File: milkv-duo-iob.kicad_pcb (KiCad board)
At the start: 2 copper layers, 71.6 x 57.7 mm, 15 parts, among them J1 8P8C_Shielded, J2 Conn_01x20, J3 Conn_01x20, J4 Conn_01x12, J5 Conn_01x12, J6 Conn_01x04, SW1 SW_Push, SW2 SW_Push, U1 Milk-V Duo

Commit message: Rev.B
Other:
- board text added: "Milk-V Duo IO Board Rev.B 2024-09-24 @myon___"
- board text removed: "Milk-V Duo IO Board Rev.A 2024-09-21 @myon___"
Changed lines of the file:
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@@
 		)
 	)
-	(gr_text "Milk-V Duo IO Board Rev.A\n2024-09-21 @myon___"
+	(gr_text "Milk-V Duo IO Board Rev.B\n2024-09-24 @myon___"
 		(at 129.54 102.87 0)
 		(layer "F.SilkS")

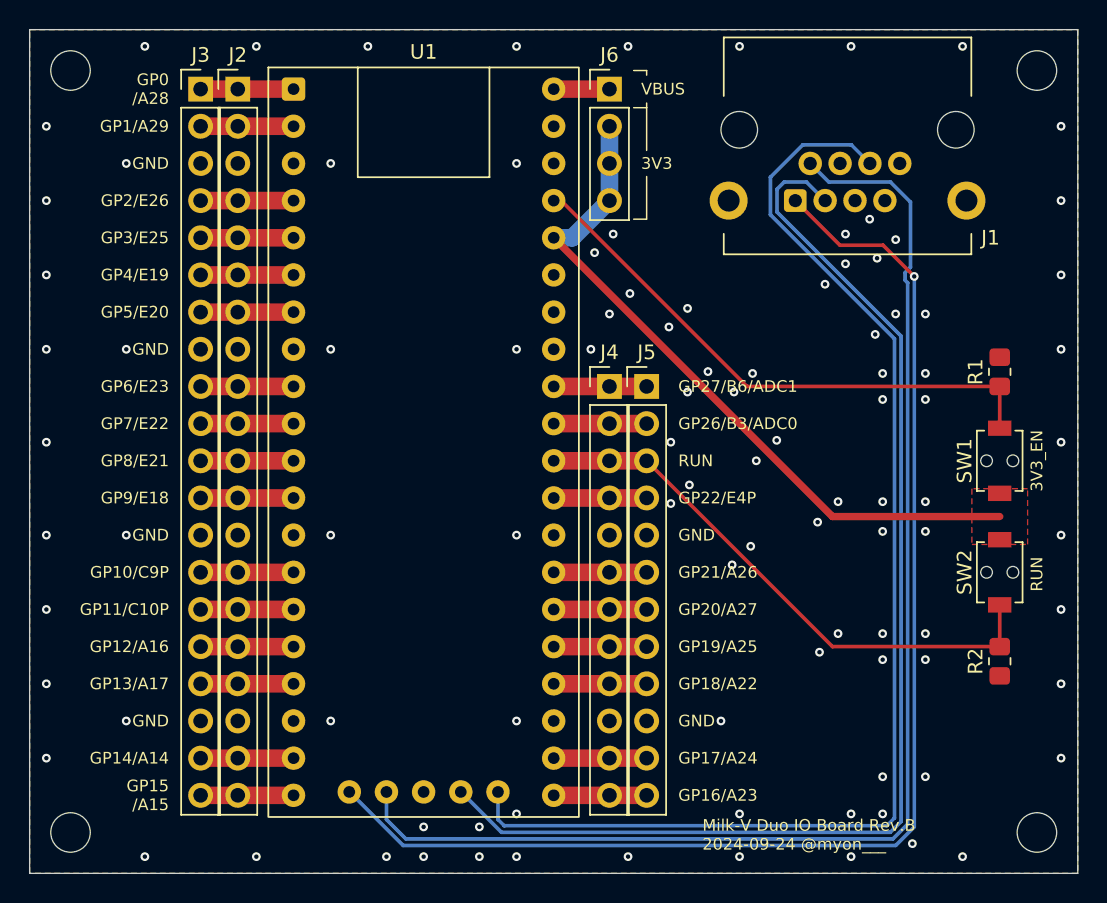
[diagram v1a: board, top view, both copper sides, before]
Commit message: Improve impedance of Etherer (hopefully)
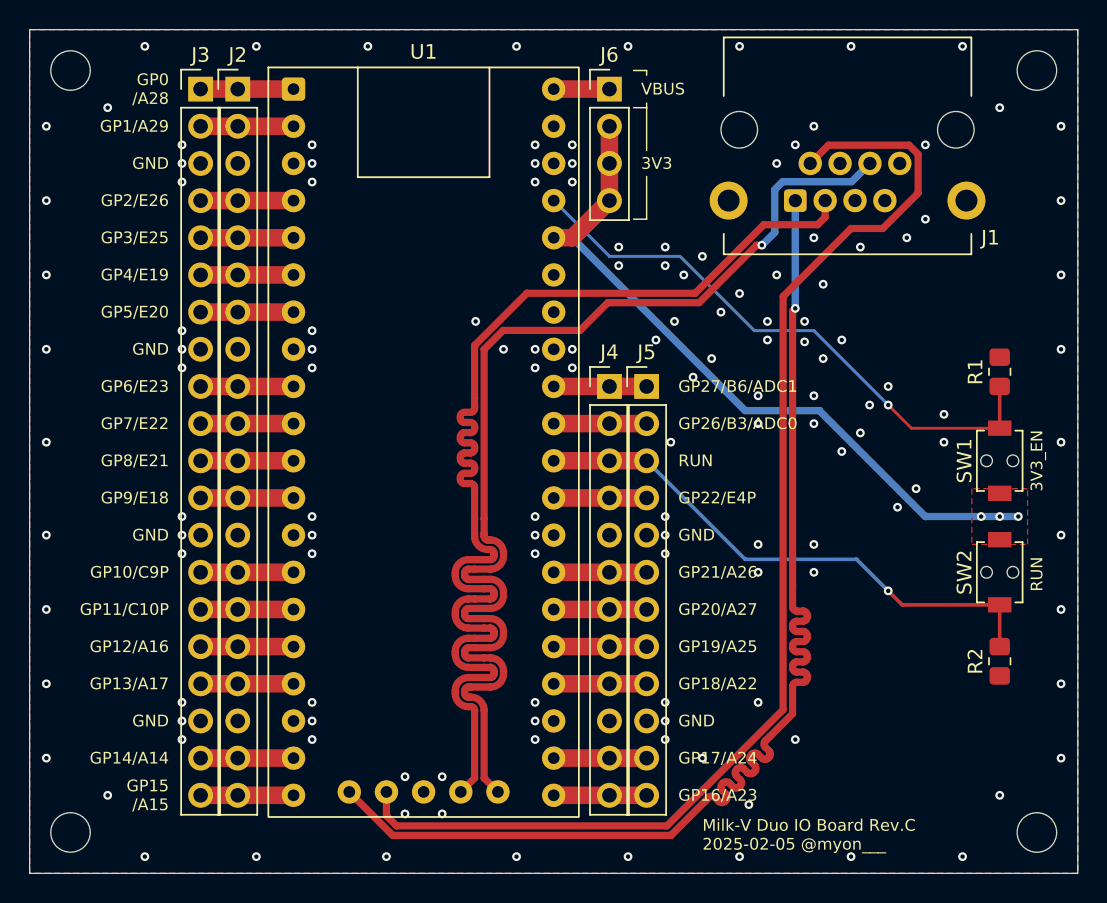
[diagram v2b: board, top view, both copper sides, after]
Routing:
- net /ETH-TX+: track 88.5 -> 81.6 mm
- net /ETH-TX-: track 89.2 -> 83.5 mm
- net /ETH-RX-: track 84.9 -> 80.3 mm, vias 0 -> 1
- net 3V3: track 48.3 -> 49.6 mm, vias 0 -> 3
- net /RUN: track 38.6 -> 37.4 mm, vias 0 -> 1
- net /3V3_EN: track 38.6 -> 39.8 mm, vias 0 -> 1
- net /ETH-RX+: track 82.3 -> 81.7 mm
- net GND: vias 101 -> 139
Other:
- board text added: "Milk-V Duo IO Board Rev.${REVISION} ${ISSUE_DATE} @myon___"
- board text removed: "Milk-V Duo IO Board Rev.B 2024-09-24 @myon___"
